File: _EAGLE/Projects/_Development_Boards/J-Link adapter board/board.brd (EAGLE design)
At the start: 40 x 60 mm, 2 parts, among them J1 AVR_SPI_PROG_5X2PTH2, J2 CORTEX_JTAG_DEBUG_PTH

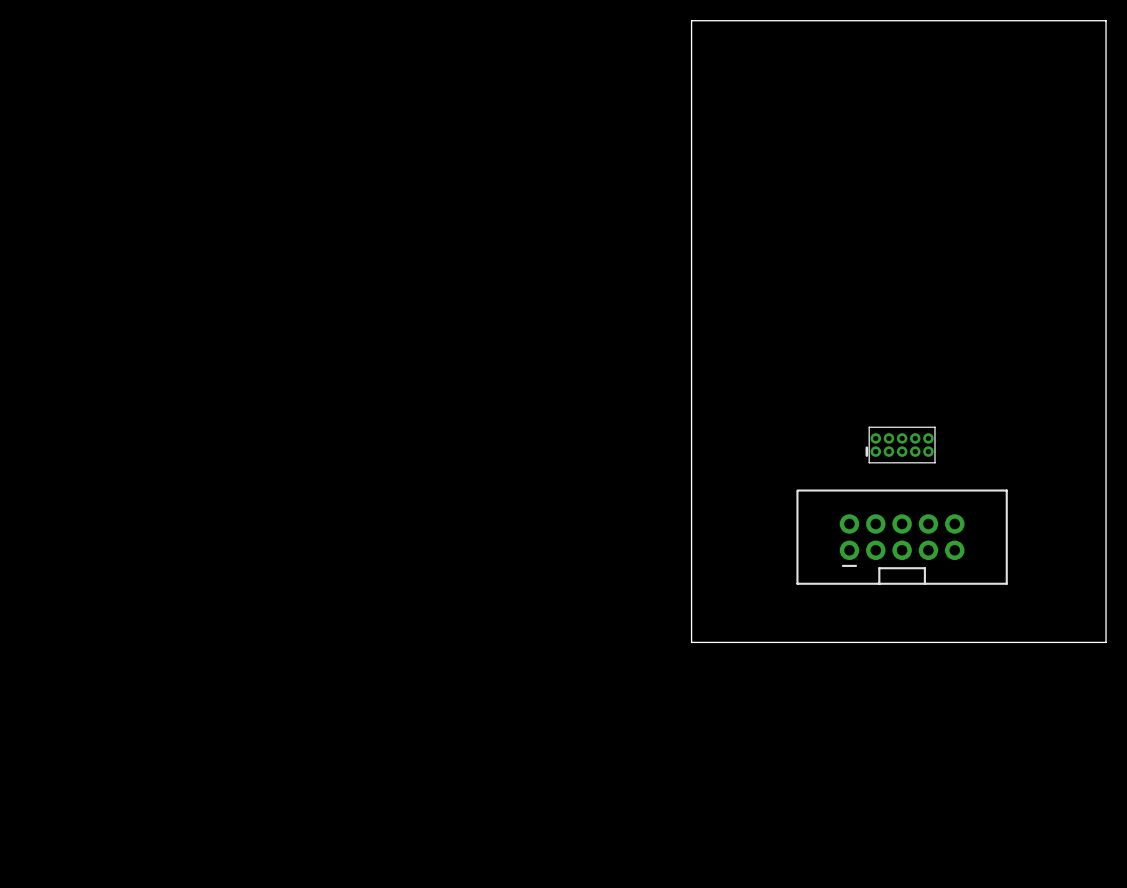
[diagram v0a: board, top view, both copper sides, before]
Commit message: PCB: programming connector lib update
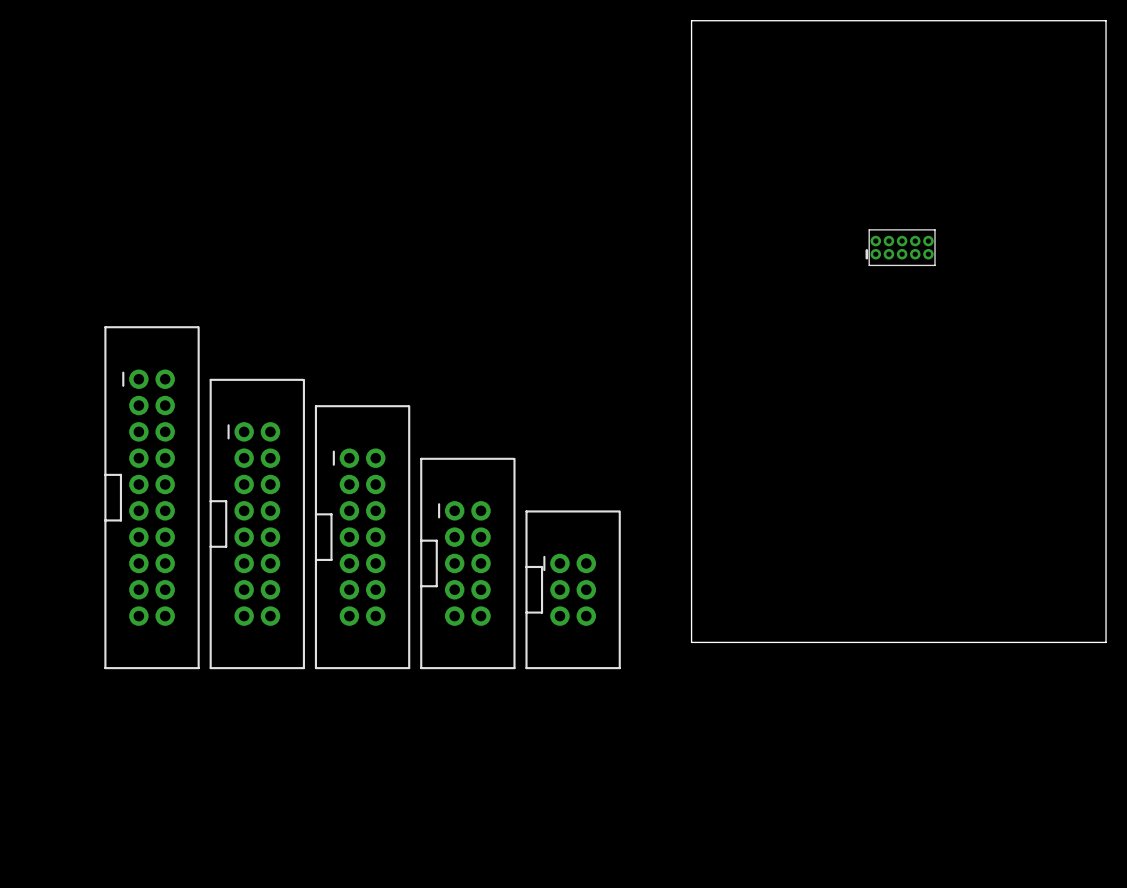
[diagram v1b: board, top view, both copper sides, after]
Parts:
- added J3: PROG-HEADER_2X5_SHROUDED, angrypig7-Connectors-Programming:2X5-2.54MM-SHROUDED
- added J4: PROG-HEADER_2X7_SHROUDED, angrypig7-Connectors-Programming:2X7-2.54MM-SHROUDED
- added J5: PROG-HEADER_2X8_SHROUDED, angrypig7-Connectors-Programming:2X8-2.54MM-SHROUDED
- added J6: PROG-HEADER_2X10_SHROUDED, angrypig7-Connectors-Programming:2X10-2.54MM-SHROUDED
- J1: value AVR_SPI_PROG_5X2PTH2 -> PROG-HEADER_2X3_SHROUDED; device angrypig7-Connectors-Programming:2X5-2.54MM-SHROUDED -> angrypig7-Connectors-Programming:2X3-2.54MM-SHROUDED
- moved J1 32.2 mm to (-11.4, 5.08), turned to 0 degrees
- moved J2 19.1 mm to (20.3, 38.1)
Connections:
- new net /JEN: J4.1
- new net /RST: J4.8
- new net /TERR: J4.14
- new net 4: J4.4
- new net BRKIN: J5.13
- new net BRKOUT: J5.10
- new net CPUCLK: J5.5
- new net N$1: J1.2, J1.3, J1.4, J1.5, J1.6, J6.1, J6.10, J6.11, J6.12, J6.13, J6.14, J6.15, J6.16, J6.17, J6.18, J6.19, J6.2, J6.20, J6.3, J6.4, J6.5, J6.6, J6.7, J6.8, J6.9
- new net OCDSE: J5.14
- new net RST: J3.10, J5.8
- new net RTCK: J3.7
- new net TCLK: J3.4, J4.11, J5.11
- new net TDI: J3.8, J4.5, J5.7
- new net TDO: J3.6, J4.13, J5.3
- new net TMS: J3.2, J4.9, J5.1
- new net TRAP: J5.15
- new net TRST: J4.2, J5.9
- new net TSTAT: J4.6
- net GND: now also J3.3, J3.5, J3.9, J4.10, J4.12, J4.3, J5.12, J5.16, J5.4, J5.6; no longer J1.10, J1.4, J1.6, J1.8
- net VCC: now also J1.1, J3.1, J4.7, J5.2; no longer J1.2
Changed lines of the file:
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@@
 </autorouter>
 <elements>
-<element name="J1" library="angrypig7-Connectors-Programming" package="2X5-2.54MM-SHROUDED" value="AVR_SPI_PROG_5X2PTH2" x="20.32" y="10.16" smashed="yes" rot="R90">
-<attribute name="PROD_ID" value="CONN-08671" x="33.02" y="29.21" size="1.778" layer="27" rot="R90" display="off"/>
-<attribute name="SF_ID" value="PRT-08506" x="33.02" y="29.21" size="1.778" layer="27" rot="R90" display="off"/>
+<element name="J2" library="angrypig7-Connectors-Programming" package="2X5-1.27MM-PTH" value="CORTEX_JTAG_DEBUG_PTH" x="20.32" y="38.1" smashed="yes"/>
+<element name="J1" library="angrypig7-Connectors-Programming" package="2X3-2.54MM-SHROUDED" value="PROG-HEADER_2X3_SHROUDED" x="-11.43" y="5.08" smashed="yes"/>
+<element name="J3" library="angrypig7-Connectors-Programming" package="2X5-2.54MM-SHROUDED" value="PROG-HEADER_2X5_SHROUDED" x="-21.59" y="7.62" smashed="yes">
+<attribute name="PROD_ID" value="CONN-08671" x="-21.59" y="7.62" size="1.778" layer="27" display="off"/>
+<attribute name="SF_ID" value="PRT-08506" x="-21.59" y="7.62" size="1.778" layer="27" display="off"/>
 </element>
-<element name="J2" library="angrypig7-Connectors-Programming" package="2X5-1.27MM-PTH" value="CORTEX_JTAG_DEBUG_PTH" x="20.32" y="19.05" smashed="yes"/>
+<element name="J4" library="angrypig7-Connectors-Programming" package="2X7-2.54MM-SHROUDED" value="PROG-HEADER_2X7_SHROUDED" x="-31.75" y="10.16" smashed="yes"/>
+<element name="J5" library="angrypig7-Connectors-Programming" package="2X8-2.54MM-SHROUDED" value="PROG-HEADER_2X8_SHROUDED" x="-41.91" y="11.43" smashed="yes"/>
+<element name="J6" library="angrypig7-Connectors-Programming" package="2X10-2.54MM-SHROUDED" value="PROG-HEADER_2X10_SHROUDED" x="-52.07" y="13.97" smashed="yes"/>
 </elements>
 <signals>
+<signal name="N$1">
+<contactref element="J1" pad="2"/>
+<contactref element="J1" pad="3"/>
+<contactref element="J1" pad="4"/>
+<contactref element="J1" pad="5"/>
+<contactref element="J1" pad="6"/>
+<contactref element="J6" pad="1"/>
+<contactref element="J6" pad="3"/>
+<contactref element="J6" pad="5"/>
+<contactref element="J6" pad="7"/>
+<contactref element="J6" pad="9"/>
+<contactref element="J6" pad="11"/>
+<contactref element="J6" pad="13"/>
+<contactref element="J6" pad="15"/>
+<contactref element="J6" pad="17"/>
+<contactref element="J6" pad="19"/>
+<contactref element="J6" pad="20"/>
+<contactref element="J6" pad="18"/>
+<contactref element="J6" pad="16"/>
+<contactref element="J6" pad="14"/>
+<contactref element="J6" pad="12"/>
+<contactref element="J6" pad="10"/>
+<contactref element="J6" pad="8"/>
+<contactref element="J6" pad="6"/>
+<contactref element="J6" pad="4"/>
+<contactref element="J6" pad="2"/>
+<wire x1="-53.34" y1="5.08" x2="-53.34" y2="2.54" width="0" layer="19" extent="1-1"/>
+<wire x1="-50.8" y1="2.54" x2="-53.34" y2="2.54" width="0" layer="19" extent="1-1"/>
+<wire x1="-53.34" y1="7.62" x2="-53.34" y2="5.08" width="0" layer="19" extent="1-1"/>
+<wire x1="-50.8" y1="5.08" x2="-53.34" y2="5.08" width="0" layer="19" extent="1-1"/>
+<wire x1="-53.34" y1="10.16" x2="-53.34" y2="7.62" width="0" layer="19" extent="1-1"/>
+<wire x1="-50.8" y1="7.62" x2="-53.34" y2="7.62" width="0" layer="19" extent="1-1"/>
+<wire x1="-53.34" y1="12.7" x2="-53.34" y2="10.16" width="0" layer="19" extent="1-1"/>
+<wire x1="-50.8" y1="10.16" x2="-53.34" y2="10.16" width="0" layer="19" extent="1-1"/>
+<wire x1="-53.34" y1="15.24" x2="-53.34" y2="12.7" width="0" layer="19" extent="1-1"/>
+<wire x1="-50.8" y1="12.7" x2="-53.34" y2="12.7" width="0" layer="19" extent="1-1"/>
+<wire x1="-53.34" y1="17.78" x2="-53.34" y2="15.24" width="0" layer="19" extent="1-1"/>
+<wire x1="-50.8" y1="15.24" x2="-53.34" y2="15.24" width="0" layer="19" extent="1-1"/>
+<wire x1="-53.34" y1="20.32" x2="-53.34" y2="17.78" width="0" layer="19" extent="1-1"/>
+<wire x1="-50.8" y1="17.78" x2="-53.34" y2="17.78" width="0" layer="19" extent="1-1"/>
+<wire x1="-53.34" y1="22.86" x2="-53.34" y2="20.32" width="0" layer="19" extent="1-1"/>
+<wire x1="-50.8" y1="20.32" x2="-53.34" y2="20.32" width="0" layer="19" extent="1-1"/>
+<wire x1="-53.34" y1="25.4" x2="-53.34" y2="22.86" width="0" layer="19" extent="1-1"/>
+<wire x1="-50.8" y1="22.86" x2="-53.34" y2="22.86" width="0" layer="19" extent="1-1"/>
+<wire x1="-50.8" y1="25.4" x2="-53.34" y2="25.4" width="0" layer="19" extent="1-1"/>
+<wire x1="-12.7" y1="2.54" x2="-50.8" y2="2.54" width="0" layer="19" extent="1-1"/>
+<wire x1="-12.7" y1="5.08" x2="-12.7" y2="2.54" width="0" layer="19" extent="1-1"/>
+<wire x1="-10.16" y1="2.54" x2="-12.7" y2="2.54" width="0" layer="19" extent="1-1"/>
+<wire x1="-10.16" y1="5.08" x2="-12.7" y2="5.08" width="0" layer="19" extent="1-1"/>
+<wire x1="-10.16" y1="7.62" x2="-10.16" y2="5.08" width="0" layer="19" extent="1-1"/>
+</signal>
 <signal name="VCC">
-<contactref element="J1" pad="2"/>
+<contactref element="J1" pad="1"/>
+<contactref element="J3" pad="1"/>
+<contactref element="J4" pad="7"/>
+<contactref element="J5" pad="2"/>
+<wire x1="-22.86" y1="12.7" x2="-33.02" y2="10.16" width="0" layer="19" extent="1-1"/>
+<wire x1="-12.7" y1="7.62" x2="-22.86" y2="12.7" width="0" layer="19" extent="1-1"/>
+<wire x1="-40.64" y1="20.32" x2="-33.02" y2="10.16" width="0" layer="19" extent="1-1"/>
+</signal>
+<signal name="TMS">
+<contactref element="J3" pad="2"/>
+<contactref element="J4" pad="9"/>
+<contactref element="J5" pad="1"/>
+<wire x1="-20.32" y1="12.7" x2="-33.02" y2="7.62" width="0" layer="19" extent="1-1"/>
+<wire x1="-43.18" y1="20.32" x2="-33.02" y2="7.62" width="0" layer="19" extent="1-1"/>
+</signal>
+<signal name="TCLK">
+<contactref element="J3" pad="4"/>
+<contactref element="J4" pad="11"/>
+<contactref element="J5" pad="11"/>
+<wire x1="-33.02" y1="5.08" x2="-43.18" y2="7.62" width="0" layer="19" extent="1-1"/>
+<wire x1="-20.32" y1="10.16" x2="-33.02" y2="5.08" width="0" layer="19" extent="1-1"/>
+</signal>
+<signal name="TDO">
+<contactref element="J3" pad="6"/>
+<contactref element="J4" pad="13"/>
+<contactref element="J5" pad="3"/>
+<wire x1="-20.32" y1="7.62" x2="-33.02" y2="2.54" width="0" layer="19" extent="1-1"/>
+<wire x1="-43.18" y1="17.78" x2="-33.02" y2="2.54" width="0" layer="19" extent="1-1"/>
+</signal>
+<signal name="TDI">
+<contactref element="J3" pad="8"/>
+<contactref element="J4" pad="5"/>
+<contactref element="J5" pad="7"/>
+<wire x1="-33.02" y1="12.7" x2="-43.18" y2="12.7" width="0" layer="19" extent="1-1"/>
+<wire x1="-20.32" y1="5.08" x2="-33.02" y2="12.7" width="0" layer="19" extent="1-1"/>
+</signal>
+<signal name="RST">
+<contactref element="J3" pad="10"/>
+<contactref element="J5" pad="8"/>
+<wire x1="-20.32" y1="2.54" x2="-40.64" y2="12.7" width="0" layer="19" extent="1-1"/>
 </signal>
 <signal name="GND">
-<contactref element="J1" pad="4"/>
-<contactref element="J1" pad="6"/>
-<contactref element="J1" pad="8"/>
-<contactref element="J1" pad="10"/>
-<wire x1="22.86" y1="11.43" x2="25.4" y2="11.43" width="0" layer="19" extent="1-1"/>
-<wire x1="20.32" y1="11.43" x2="22.86" y2="11.43" width="0" layer="19" extent="1-1"/>
-<wire x1="17.78" y1="11.43" x2="20.32" y2="11.43" width="0" layer="19" extent="1-1"/>
+<contactref element="J3" pad="3"/>
+<contactref element="J3" pad="5"/>
+<contactref element="J3" pad="9"/>
+<contactref element="J4" pad="3"/>
+<contactref element="J4" pad="10"/>
+<contactref element="J4" pad="12"/>
+<contactref element="J5" pad="4"/>
+<contactref element="J5" pad="6"/>
+<contactref element="J5" pad="12"/>
+<contactref element="J5" pad="16"/>
+<wire x1="-40.64" y1="7.62" x2="-40.64" y2="2.54" width="0" layer="19" extent="1-1"/>
+<wire x1="-40.64" y1="15.24" x2="-40.64" y2="7.62" width="0" layer="19" extent="1-1"/>
+<wire x1="-40.64" y1="17.78" x2="-40.64" y2="15.24" width="0" layer="19" extent="1-1"/>
+<wire x1="-33.02" y1="15.24" x2="-40.64" y2="15.24" width="0" layer="19" extent="1-1"/>
+<wire x1="-30.48" y1="7.62" x2="-33.02" y2="15.24" width="0" layer="19" extent="1-1"/>
+<wire x1="-30.48" y1="5.08" x2="-30.48" y2="7.62" width="0" layer="19" extent="1-1"/>
+<wire x1="-22.86" y1="7.62" x2="-30.48" y2="7.62" width="0" layer="19" extent="1-1"/>
+<wire x1="-22.86" y1="10.16" x2="-22.86" y2="7.62" width="0" layer="19" extent="1-1"/>
+<wire x1="-22.86" y1="2.54" x2="-22.86" y2="7.62" width="0" layer="19" extent="1-1"/>
+</signal>
+<signal name="RTCK">
+<contactref element="J3" pad="7"/>
+</signal>
+<signal name="/JEN">
+<contactref element="J4" pad="1"/>
+</signal>
+<signal name="TRST">
+<contactref element="J4" pad="2"/>
+<contactref element="J5" pad="9"/>
+<wire x1="-30.48" y1="17.78" x2="-43.18" y2="10.16" width="0" layer="19" extent="1-1"/>
+</signal>
+<signal name="4">
+<contactref element="J4" pad="4"/>
+</signal>
+<signal name="TSTAT">
+<contactref element="J4" pad="6"/>
+</signal>
+<signal name="/RST">
+<contactref element="J4" pad="8"/>
+</signal>
+<signal name="/TERR">
+<contactref element="J4" pad="14"/>
+</signal>
+<signal name="CPUCLK">
+<contactref element="J5" pad="5"/>
+</signal>
+<signal name="BRKIN">
+<contactref element="J5" pad="13"/>
+</signal>
+<signal name="TRAP">
+<contactref element="J5" pad="15"/>
+</signal>
+<signal name="BRKOUT">
+<contactref element="J5" pad="10"/>
+</signal>
+<signal name="OCDSE">
+<contactref element="J5" pad="14"/>
 </signal>
 </signals>

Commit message: PCB: conn lib update, j-link adapter board schematics somewhat done
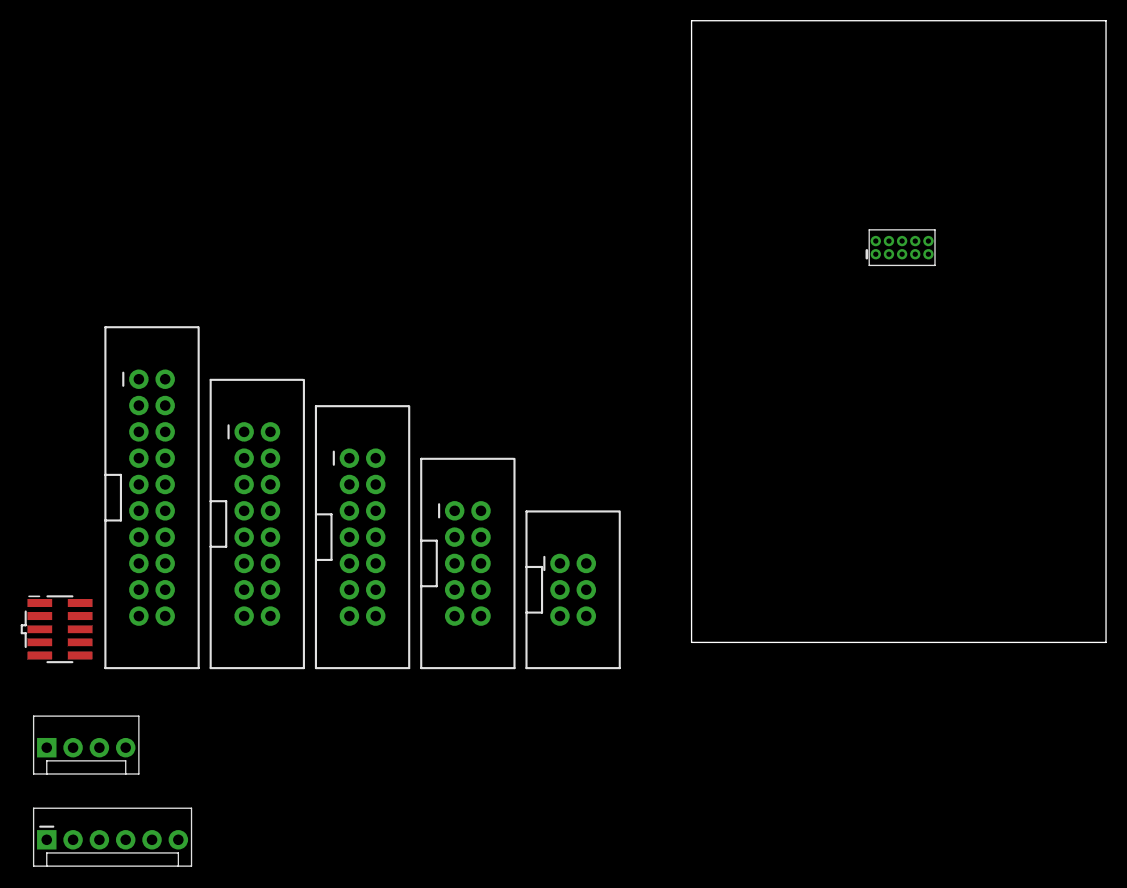
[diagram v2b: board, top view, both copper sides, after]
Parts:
- added J7: PROG-HEADER_2X5_1.27MM-SMD, angrypig7-Connectors-Programming:2X3-1.27MM_SMD
- added J8: CONN-1X4, angrypig7-Connectors-Programming:MOLEX-1X4
- added J9: CONN-1X6, angrypig7-Connectors-Programming:MOLEX-1X6
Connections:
- removed net N$1: J1.2, J1.3, J1.4, J1.5, J1.6, J6.1, J6.10, J6.11, J6.12, J6.13, J6.14, J6.15, J6.16, J6.17, J6.18, J6.19, J6.2, J6.20, J6.3, J6.4, J6.5, J6.6, J6.7, J6.8, J6.9
- removed net TCLK: J3.4, J4.11, J5.11
- new net TCK: J3.4, J4.11, J5.11, J6.9, J7.4, J8.3, J9.3
- net GND: now also J1.1, J1.2, J1.3, J1.4, J1.5, J1.6, J6.10, J6.12, J6.14, J6.16, J6.18, J6.20, J6.4, J6.6, J6.8, J7.3, J7.5, J7.9, J8.4, J9.1
- net RST: now also J6.15, J7.10, J9.5
- net RTCK: now also J6.11, J7.7
- net TDI: now also J6.5, J7.8
- net TDO: now also J6.13, J7.6, J9.4
- net TMS: now also J6.7, J7.2, J8.2, J9.2
- net TRST: now also J6.3
- net VCC: now also J6.1, J6.2, J7.1, J8.1, J9.6; no longer J1.1

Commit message: PCB lib update, J-Link adapter pcb update
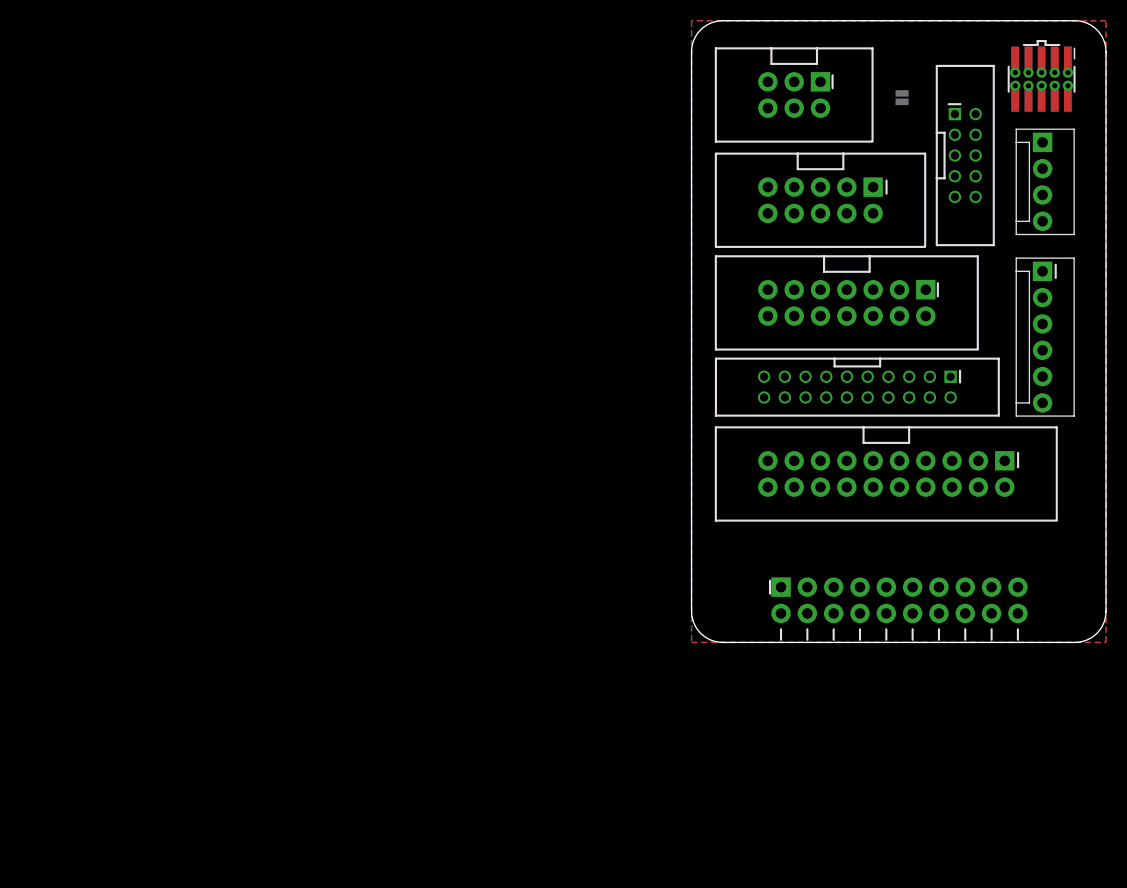
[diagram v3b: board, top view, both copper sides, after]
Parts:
- added J10: PROG-HEADER_2X5_1.27MM-PTH+SMD, angrypig7-Connectors-Programming:2X5-1.27MM_PTH+SMD
- added JP1: TCK-RTCK, SparkFun-Jumpers:SMT-JUMPER_2_NO_SILK
- J2: value CORTEX_JTAG_DEBUG_PTH -> PROG-HEADER_2X5_2.00MM-SHROUDED; device angrypig7-Connectors-Programming:2X5-1.27MM-PTH -> angrypig7-Connectors-Programming:2X5-2.00MM-SHROUDED
- J5: value PROG-HEADER_2X8_SHROUDED -> PROG-HEADER_2X10_RIGHT-ANGLE; device angrypig7-Connectors-Programming:2X8-2.54MM-SHROUDED -> angrypig7-Connectors-Programming:2X10-2.54MM-RIGHT-ANGLE
- J7: value PROG-HEADER_2X5_1.27MM-SMD -> PROG-HEADER_2X10_2.00MM-SHROUDED; device angrypig7-Connectors-Programming:2X3-1.27MM_SMD -> angrypig7-Connectors-Programming:2X10-2.00MM-SHROUDED
- J8: device angrypig7-Connectors-Programming:MOLEX-1X4 -> angrypig7-Connectors-Programming:MOLEX-1X4-2.54MM
- J9: device angrypig7-Connectors-Programming:MOLEX-1X6 -> angrypig7-Connectors-Programming:MOLEX-1X6-2.54MM
- moved J8 112.5 mm to (33.9, 48.3), turned to 270 degrees
- moved J9 110.7 mm to (33.9, 35.8), turned to 270 degrees
- moved J7 80.4 mm to (16.0, 24.6)
- moved J6 70.9 mm to (18.8, 16.3), turned to 270 degrees
- moved J5 62.4 mm to (20.1, 4.06), turned to 90 degrees
- moved J1 52.3 mm to (9.91, 52.8), turned to 270 degrees
- moved J4 51.9 mm to (15.0, 32.8), turned to 270 degrees
- moved J3 48.9 mm to (12.4, 42.7), turned to 270 degrees
- moved J2 10.8 mm to (26.4, 47.0)
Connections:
- removed net BRKIN: J5.13
- removed net BRKOUT: J5.10
- removed net CPUCLK: J5.5
- removed net OCDSE: J5.14
- removed net TRAP: J5.15
- new net (VCC): J5.2, J6.2, J7.2
- net GND: now also J10.13, J10.15, J10.19, J10.3, J10.5, J10.9, J2.3, J2.5, J2.9, J5.10, J5.14, J5.18, J5.20, J5.8, J7.10, J7.12, J7.14, J7.16, J7.18, J7.20, J7.4, J7.6, J7.8; no longer J1.1, J1.2, J1.3, J1.4, J1.6, J7.3, J7.5, J7.9
- net RST: now also J1.3, J10.10, J10.20, J2.10, J5.15, J7.15; no longer J5.8, J7.10
- net RTCK: now also J10.17, J10.7, J2.7, J5.11, J7.11, JP1.2; no longer J7.7
- net TCK: now also J1.4, J10.14, J10.4, J2.4, J5.9, J7.9, JP1.1; no longer J5.11, J7.4
- net TDI: now also J10.18, J10.8, J2.8, J5.5, J7.5; no longer J5.7, J7.8
- net TDO: now also J1.6, J10.16, J10.6, J2.6, J5.13, J7.13; no longer J5.3, J7.6
- net TMS: now also J1.2, J10.12, J10.2, J2.2, J5.7, J7.7; no longer J5.1, J7.2
- net TRST: now also J5.3, J7.3; no longer J5.9
- net VCC: now also J1.1, J10.1, J10.11, J2.1, J5.1; no longer J5.2, J6.2
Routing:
- added copper zone on layer 1, net GND
- added copper zone on layer 16, net GND
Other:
- outline, holes or cut-outs redrawn
- board text added: ">CNAME"
- board text added: ">CREVISION"
- board text added: ">GITHUB"
- board text added: "GND"
- board text added: "RST"
- board text added: "RTCK"
- board text added: "TCK"
- board text added: "TCK - SWDCLK"
- board text added: "TDI"
- board text added: "TDO"
- board text added: "TDO - SWO"
- board text added: "TMS"
- board text added: "TMS - SWDIO"
- board text added: "TRST"
- board text added: "VCC"
